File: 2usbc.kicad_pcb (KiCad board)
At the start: 4 copper layers, 26 x 30 mm, 71 parts, among them J101 USB_C_Plug_USB2.0, J102 USB_C_Receptacle_USB2.0, J103 USB_C_Receptacle_USB2.0, U101 TLV76733DRVx, U102 USBLC6-2SC6, U201 USB2512B, U301 USBLC6-2SC6, U302 MIC2097-1YMT-TR, U303 TUSB320, U304 AP2161W, U401 USBLC6-2SC6, U402 MIC2097-1YMT-TR, U403 TUSB320, U404 AP2161W, Y201 24MHz

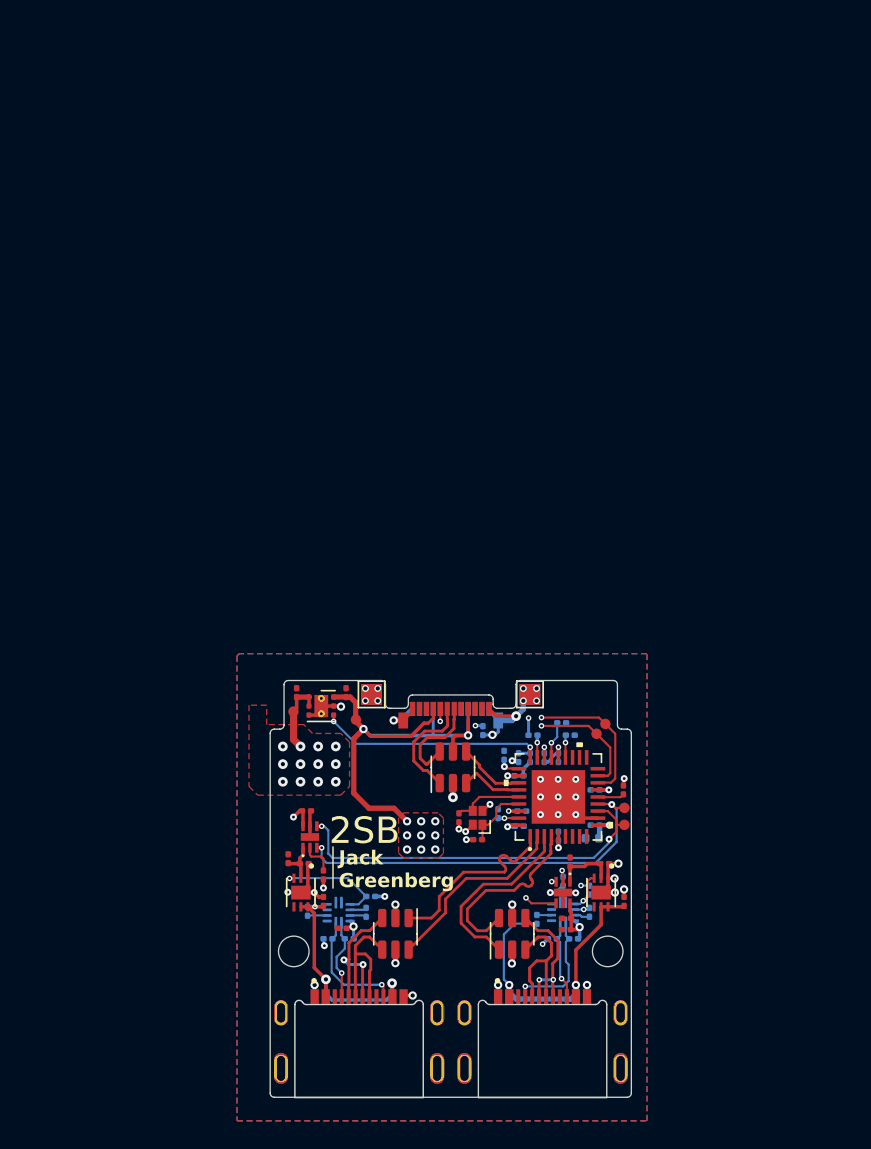
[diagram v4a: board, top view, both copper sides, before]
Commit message: Update schematic with feedback
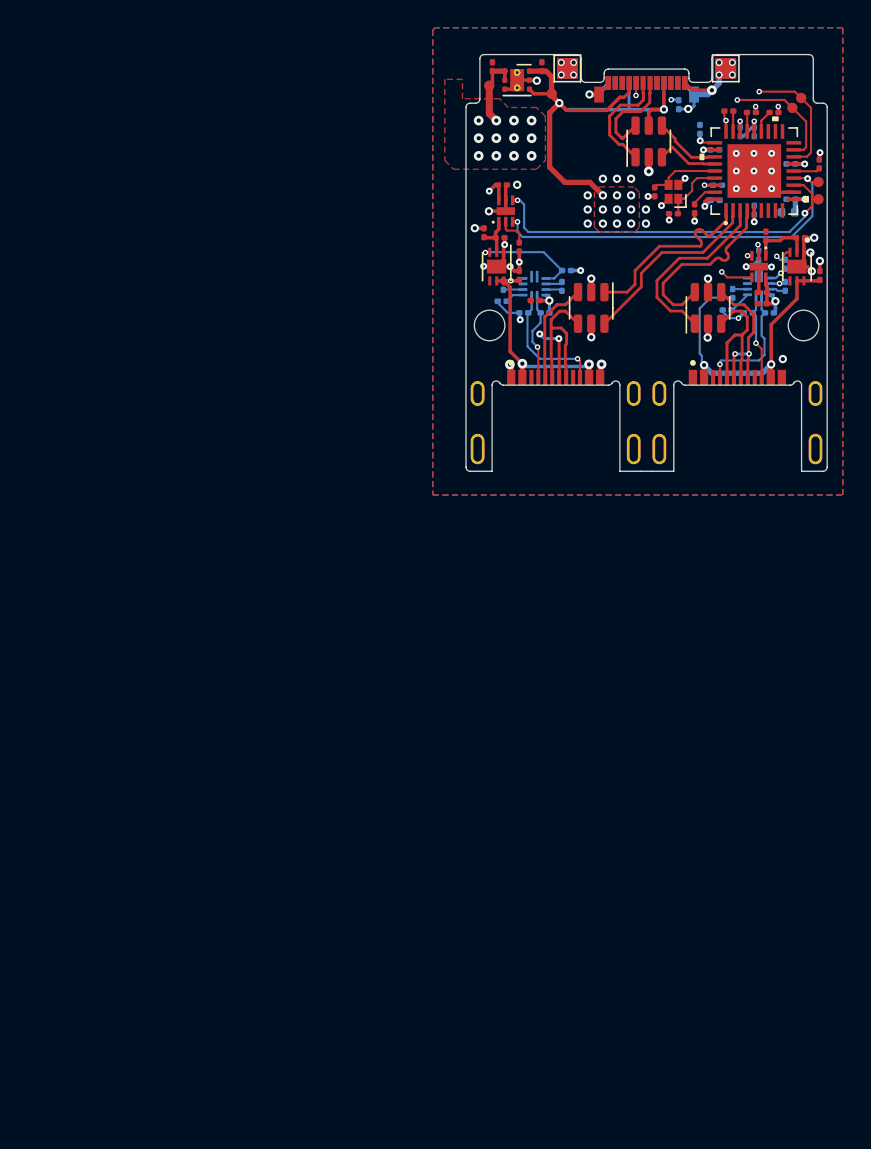
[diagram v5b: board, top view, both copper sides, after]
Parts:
- removed R202, R203: 100K, Resistor_SMD:R_0201_0603Metric
- added R307: 10k, Resistor_SMD:R_0201_0603Metric, B.Cu at (143.7, 99.7)
- added R407: 10k, Resistor_SMD:R_0201_0603Metric, B.Cu at (159.9, 100.3)
- J102, J103: footprint 2usb:MOLEX_2169900003 -> 2usb:USB4520
- R201, R204, R206, R208: moved to F.Cu
- U302, U402: value MIC2097-1YMT-TR -> TMLF-6_MT_MCH
- moved J102 51.2 mm to (147.6, 105.7)
- moved J103 51.1 mm to (160.6, 105.7)
- moved R301 47.3 mm to (144.9, 95.8)
- moved C301 47.3 mm to (146.1, 99.6)
- moved R402 47.2 mm to (162.9, 100.5)
- moved R403 47.2 mm to (161.4, 100.5)
- moved U302 47.2 mm to (144.0, 93.2)
- moved R205 47.2 mm to (157.9, 87.3)
- moved R302 47.2 mm to (146.8, 100.5)
- moved R303 47.2 mm to (145.3, 100.5)
- moved C102 47.2 mm to (143.0, 82.8)
- moved C201 47.2 mm to (161.8, 93.1)
- moved C207 47.2 mm to (161.8, 87.5)
- moved C210 47.2 mm to (164.3, 93.3)
- moved C211 47.2 mm to (159.2, 91.3)
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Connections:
- U101 pad 4: VBUS_DET -> VBUS
- U201 pad 27: VBUS_DET -> +3V3
- U303 pad 3: unconnected-(U303-PORT-Pad3) -> /Output Stage 1/PORT
- U403 pad 3: unconnected-(U403-PORT-Pad3) -> /Output Stage 2/PORT
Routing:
- net VBUS_DET: track 17.4 -> 0.00 mm, vias 2 -> 0
- net VBUS: track 47.9 -> 53.3 mm
- net GND: track 46.5 -> 49.7 mm, vias 43 -> 57
- net /Output Stage 2/PORT: track 0.00 -> 1.61 mm
- net /P1_VBUS: track 17.2 -> 15.6 mm
- net /Output Stage 1/PORT: track 0.00 -> 1.36 mm
- net Net-(U201-SCL/SMBCLK/CFG_SEL0): track 2.66 -> 1.38 mm, vias 1 -> 0
- net /Output Stage 1/OUT_USB_DN: track 11.3 -> 12.3 mm
- net /Output Stage 1/OUT_USB_DP: track 10.3 -> 11.3 mm
- net /Output Stage 2/OUT_USB_DP: track 9.48 -> 10.5 mm
- net /Output Stage 2/OUT_USB_DN: track 10.0 -> 10.8 mm
- net /P2_CC1: track 8.54 -> 9.05 mm
- net Net-(U201-RBIAS): track 1.50 -> 1.88 mm, vias 1 -> 0
- net +3V3: track 22.0 -> 22.4 mm, vias 20 -> 19
- net /Hub IC/~{RESET}: track 1.60 -> 1.48 mm, vias 1 -> 0
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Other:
- outline, holes or cut-outs redrawn
- board text added: "frame.work"
- board text removed: "SIG GND PWR PWR GND SIG"
- board text removed: "frame .work"
